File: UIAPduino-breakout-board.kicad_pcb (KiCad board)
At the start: 2 copper layers, 56.6 x 54.1 mm, 13 parts, among them J1 Conn_01x20_Pin, J2 Conn_01x20_Socket, J3 Barrel_Jack_Switch, U3 L7805

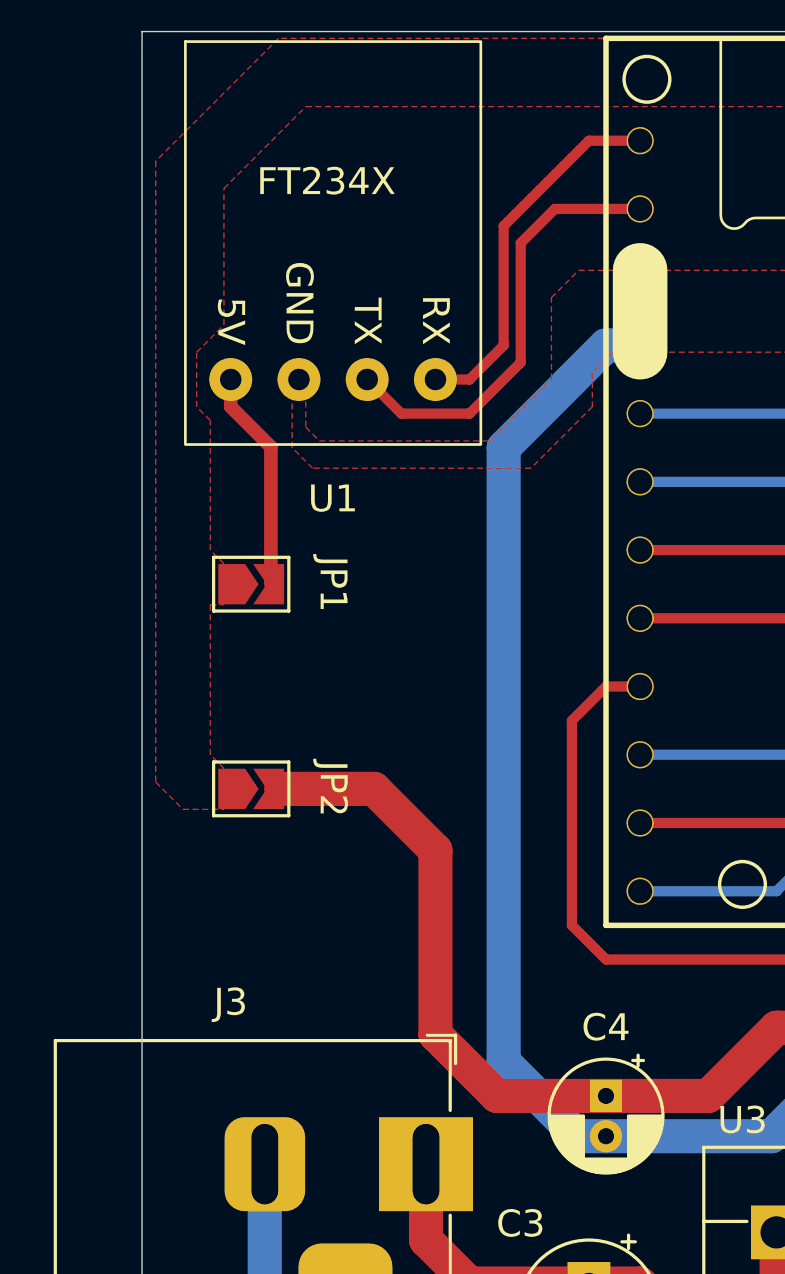
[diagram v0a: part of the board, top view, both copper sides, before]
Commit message: ジャンパをスイッチに変更
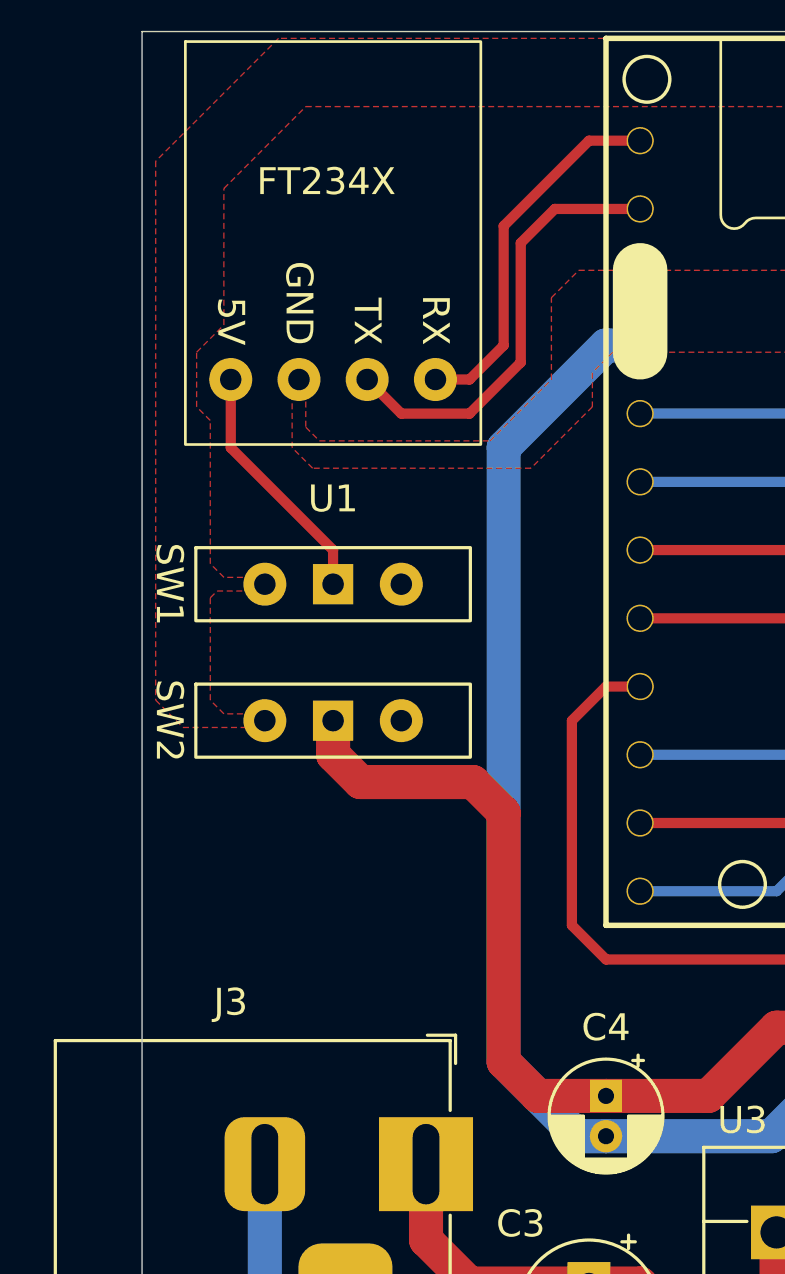
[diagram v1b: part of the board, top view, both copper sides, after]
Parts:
- removed JP1, JP2: Jumper_2_Open, Jumper:SolderJumper-2_P1.3mm_Open_TrianglePad1.0x1.5mm
- added SW1: SW_SPDT_312, Button_Switch_THT:SW_Slide-03_Wuerth-WS-SLTV_10x2.5x6.4_P2.54mm, F.Cu at (133.3, 83.8)
- added SW2: SW_SPDT_312, Button_Switch_THT:SW_Slide-03_Wuerth-WS-SLTV_10x2.5x6.4_P2.54mm, F.Cu at (133.3, 88.9)
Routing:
- net Net-(D1-A): track 45.1 -> 46.3 mm
- net Net-(SW1-B): track 8.24 -> 9.20 mm

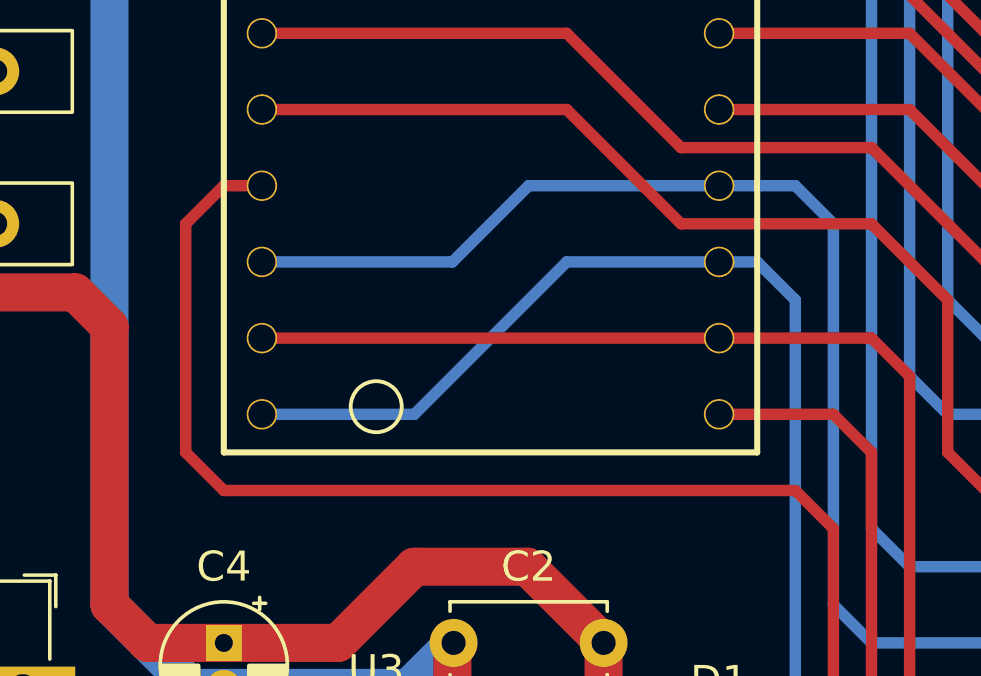
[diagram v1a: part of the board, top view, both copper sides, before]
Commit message: なくていい配線を削除
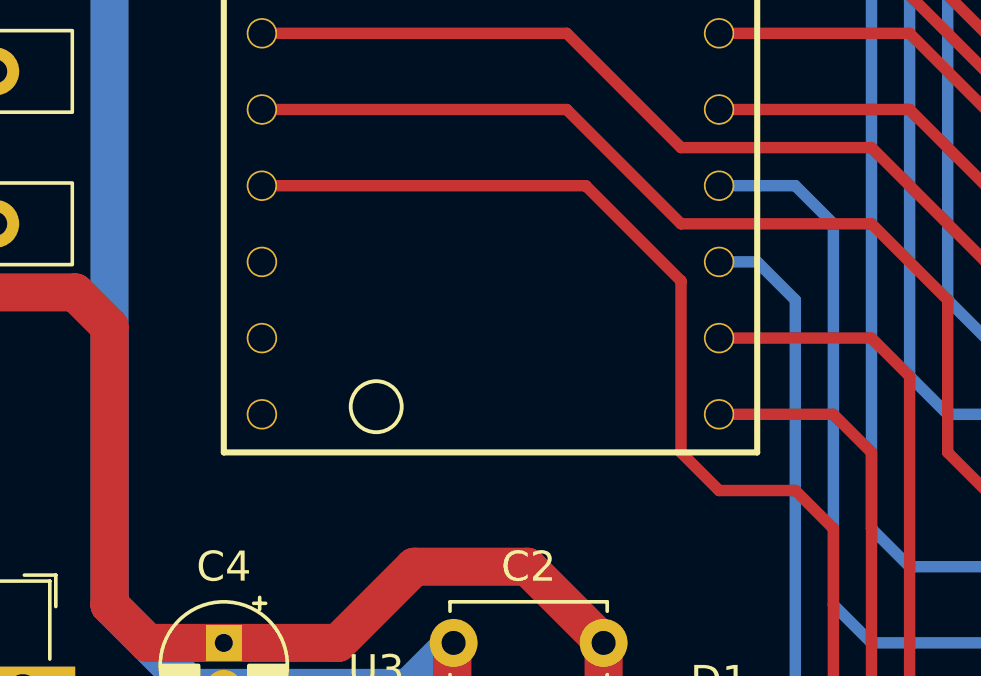
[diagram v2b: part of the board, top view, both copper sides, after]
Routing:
- net Net-(J1-Pin_17): track 55.2 -> 37.9 mm
- net Net-(J1-Pin_15): track 51.6 -> 35.3 mm
- net Net-(J1-Pin_16): track 48.0 -> 32.8 mm
- net Net-(J1-Pin_19): track 64.3 -> 58.1 mm
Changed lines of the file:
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@@
-	)
-	(segment
-		(start 144.78 90.17)
-		(end 151.13 90.17)
-		(width 0.381)
-		(layer "B.Cu")
-		(net 4)
 	)
 	(segment
@@
 	)
 	(segment
-		(start 153.67 87.63)
-		(end 160.02 87.63)
-		(width 0.381)
-		(layer "B.Cu")
-		(net 4)
-	)
-	(segment
-		(start 151.13 90.17)
-		(end 153.67 87.63)
-		(width 0.381)
-		(layer "B.Cu")
-		(net 4)
-	)
-	(segment
 		(start 171.45 102.87)
 		(end 165.1 102.87)
@@
 	)
 	(segment
+		(start 144.78 87.63)
+		(end 155.575 87.63)
+		(width 0.381)
+		(layer "F.Cu")
+		(net 6)
+	)
+	(segment
+		(start 160.02 97.79)
+		(end 162.56 97.79)
+		(width 0.381)
+		(layer "F.Cu")
+		(net 6)
+	)
+	(segment
+		(start 155.575 87.63)
+		(end 158.75 90.805)
+		(width 0.381)
+		(layer "F.Cu")
+		(net 6)
+	)
+	(segment
+		(start 163.83 99.06)
+		(end 163.83 111.76)
+		(width 0.381)
+		(layer "F.Cu")
+		(net 6)
+	)
+	(segment
 		(start 163.83 111.76)
 		(end 165.1 113.03)
@@
 	)
 	(segment
-		(start 144.78 87.63)
-		(end 143.51 87.63)
-		(width 0.381)
-		(layer "F.Cu")
-		(net 6)
-	)
-	(segment
-		(start 142.24 88.9)
-		(end 142.24 96.520168)
-		(width 0.381)
-		(layer "F.Cu")
-		(net 6)
-	)
-	(segment
-		(start 143.51 87.63)
-		(end 142.24 88.9)
-		(width 0.381)
-		(layer "F.Cu")
-		(net 6)
-	)
-	(segment
-		(start 142.24 96.520168)
-		(end 143.509832 97.79)
+		(start 158.75 90.805)
+		(end 158.75 96.52)
+		(width 0.381)
+		(layer "F.Cu")
+		(net 6)
+	)
+	(segment
+		(start 165.1 113.03)
+		(end 171.45 113.03)
 		(width 0.381)
 		(layer "F.Cu")
@@
 	)
 	(segment
-		(start 162.56 97.79)
-		(end 143.509832 97.79)
-		(width 0.381)
-		(layer "F.Cu")
-		(net 6)
-	)
-	(segment
-		(start 165.1 113.03)
-		(end 171.45 113.03)
-		(width 0.381)
-		(layer "F.Cu")
-		(net 6)
-	)
-	(segment
-		(start 163.83 99.06)
-		(end 163.83 111.76)
+		(start 158.75 96.52)
+		(end 160.02 97.79)
 		(width 0.381)
 		(layer "F.Cu")
@@
 	)
 	(segment
-		(start 154.94 90.17)
-		(end 149.86 95.25)
-		(width 0.381)
-		(layer "B.Cu")
-		(net 12)
-	)
-	(segment
 		(start 160.02 90.17)
 		(end 161.29 90.17)
@@
 	)
 	(segment
-		(start 160.02 90.17)
-		(end 154.94 90.17)
-		(width 0.381)
-		(layer "B.Cu")
-		(net 12)
-	)
-	(segment
 		(start 162.56 106.68)
 		(end 162.56 91.44)
@@
 	)
 	(segment
-		(start 149.86 95.25)
-		(end 144.78 95.25)
-		(width 0.381)
-		(layer "B.Cu")
-		(net 12)
-	)
-	(segment
 		(start 171.45 110.49)
 		(end 166.37 110.49)
@@
 		(width 0.381)
 		(layer "F.Cu")
-		(net 14)
-	)
-	(segment
-		(start 160.02 92.71)
-		(end 144.78 92.71)
-		(width 0.381)
-		(layer "F.Cu")

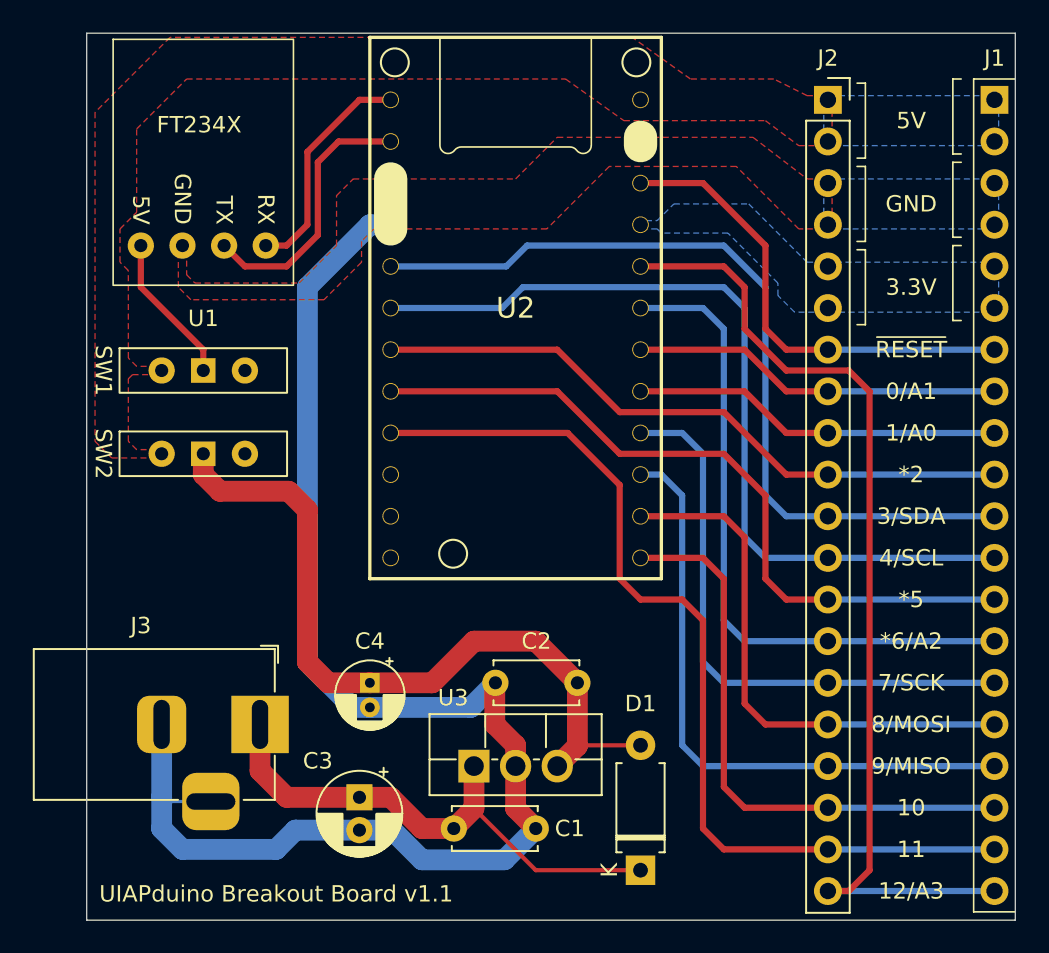
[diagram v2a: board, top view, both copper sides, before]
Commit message: UART 接続先切り替え用スイッチを追加
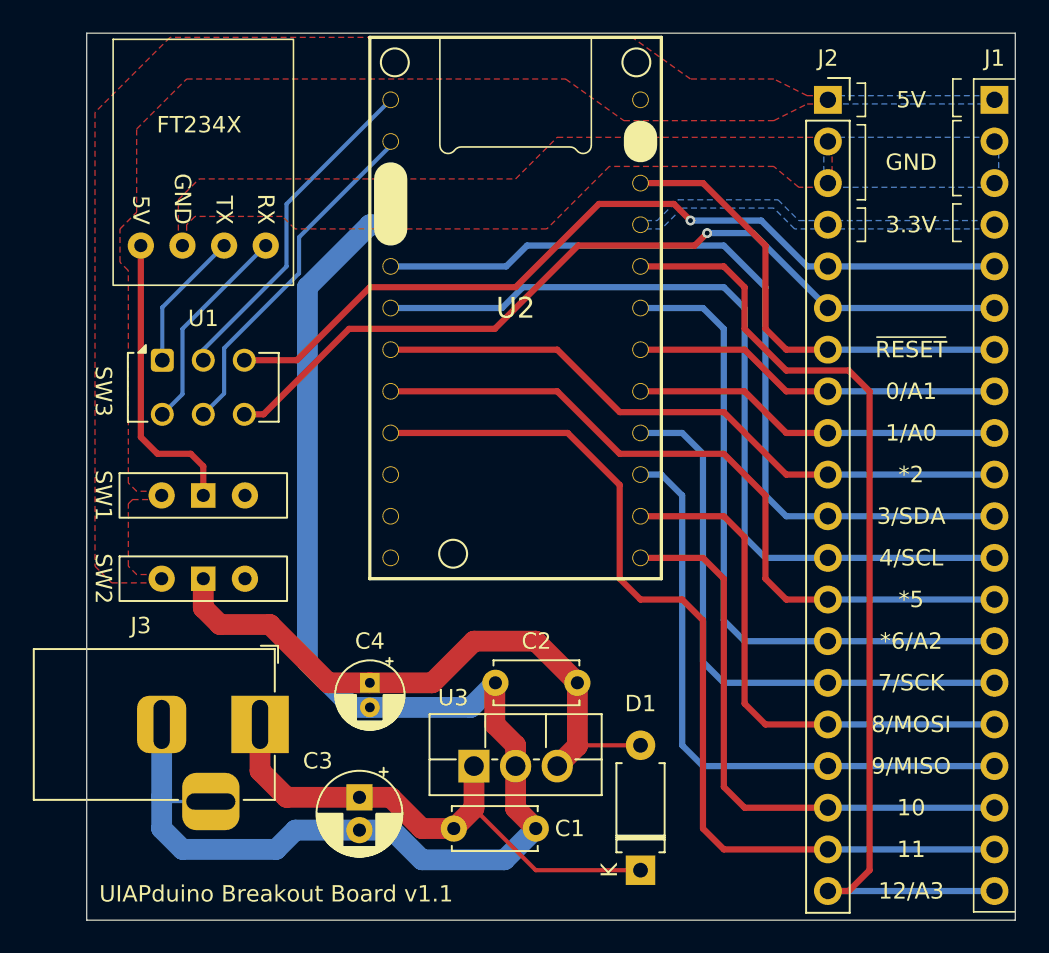
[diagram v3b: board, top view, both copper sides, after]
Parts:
- added SW3: SW_Slide_DPDT, Button_Switch_THT:SW_CK_JS202011CQN_DPDT_Straight, F.Cu at (130.8, 83.2)
- moved SW1 7.62 mm to (133.3, 91.4)
- moved SW2 7.62 mm to (133.3, 96.5)
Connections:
- J1 pad 2: +5V -> GND
- J1 pad 4: GND -> +3.3V
- J1 pad 5: +3.3V -> /EXT_TX
- J1 pad 6: +3.3V -> /EXT_RX
- J2 pad 2: +5V -> GND
- J2 pad 4: GND -> +3.3V
- J2 pad 5: +3.3V -> /EXT_TX
- J2 pad 6: +3.3V -> /EXT_RX
- U1 pad 3: Net-(U1-TX) -> /USB_TX
- U1 pad 4: Net-(U1-RX) -> /USB_RX
- U2 pad 1: Net-(U1-RX) -> /UIAP_TX
- U2 pad 2: Net-(U1-TX) -> /UIAP_RX
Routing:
- net /EXT_RX: track 0.00 -> 52.2 mm, vias 0 -> 1
- net /EXT_TX: track 0.00 -> 51.4 mm, vias 0 -> 1
- net /UIAP_RX: track 0.00 -> 21.4 mm
- net /UIAP_TX: track 0.00 -> 20.6 mm
- net Net-(U1-TX): track 16.4 -> 0.00 mm
- net Net-(U1-RX): track 13.9 -> 0.00 mm
- net /USB_RX: track 0.00 -> 12.9 mm
- net Net-(SW1-B): track 9.20 -> 18.0 mm
- net /USB_TX: track 0.00 -> 8.56 mm
- net Net-(D1-A): track 46.3 -> 38.1 mm

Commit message: 電源配線ちょい弄り
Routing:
- net GND: track 87.5 -> 80.5 mm
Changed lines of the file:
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@@
 	)
 	(segment
-		(start 131.065 110.11)
-		(end 130.81 109.855)
-		(width 0.2)
-		(layer "B.Cu")
-		(net 3)
-	)
-	(segment
-		(start 137.795 113.03)
-		(end 138.97 111.855)
-		(width 1.27)
-		(layer "B.Cu")
-		(net 3)
-	)
-	(segment
-		(start 130.81 109.855)
-		(end 130.81 111.76)
-		(width 1.27)
-		(layer "B.Cu")
-		(net 3)
-	)
-	(segment
-		(start 138.97 111.855)
+		(start 143.51 74.93)
+		(end 144.78 74.93)
+		(width 1.27)
+		(layer "B.Cu")
+		(net 3)
+	)
+	(segment
+		(start 139.541 111.855)
 		(end 142.875 111.855)
 		(width 1.27)
@@
 	)
 	(segment
-		(start 139.7 78.74)
-		(end 143.51 74.93)
+		(start 142.47 104.37)
+		(end 141.224 103.124)
+		(width 1.27)
+		(layer "B.Cu")
+		(net 3)
+	)
+	(segment
+		(start 130.81 105.41)
+		(end 130.81 108.966)
+		(width 1.27)
+		(layer "B.Cu")
+		(net 3)
+	)
+	(segment
+		(start 130.81 108.966)
+		(end 131.954 110.11)
 		(width 1.27)
 		(layer "B.Cu")
@@
 	)
 	(segment
-		(start 132.08 113.03)
-		(end 137.795 113.03)
-		(width 1.27)
-		(layer "B.Cu")
-		(net 3)
-	)
-	(segment
-		(start 133.81 110.11)
-		(end 131.065 110.11)
-		(width 0.2)
-		(layer "B.Cu")
-		(net 3)
-	)
-	(segment
-		(start 139.7 101.6)
-		(end 139.7 78.74)
-		(width 1.27)
-		(layer "B.Cu")
-		(net 3)
-	)
-	(segment
-		(start 130.81 105.41)
-		(end 130.81 109.855)
-		(width 1.27)
-		(layer "B.Cu")
-		(net 3)
-	)
-	(segment
-		(start 142.47 104.37)
-		(end 139.7 101.6)
+		(start 141.224 103.124)
+		(end 141.224 77.216)
+		(width 1.27)
+		(layer "B.Cu")
+		(net 3)
+	)
+	(segment
+		(start 141.224 77.216)
+		(end 143.51 74.93)
 		(width 1.27)
 		(layer "B.Cu")
@@
 	)
 	(segment
+		(start 131.954 110.11)
+		(end 137.796 110.11)
+		(width 1.27)
+		(layer "B.Cu")
+		(net 3)
+	)
+	(segment
+		(start 146.685 113.665)
+		(end 151.725 113.665)
+		(width 1.27)
+		(layer "B.Cu")
+		(net 3)
+	)
+	(segment
+		(start 137.796 110.11)
+		(end 139.541 111.855)
+		(width 1.27)
+		(layer "B.Cu")
+		(net 3)
+	)
+	(segment
 		(start 143.51 104.37)
 		(end 142.47 104.37)
@@
 	)
 	(segment
-		(start 146.685 113.665)
-		(end 151.725 113.665)
-		(width 1.27)
-		(layer "B.Cu")
-		(net 3)
-	)
-	(segment
-		(start 143.51 74.93)
-		(end 144.78 74.93)
-		(width 1.27)
-		(layer "B.Cu")
-		(net 3)
-	)
-	(segment
 		(start 151.17 102.87)
 		(end 149.67 104.37)
@@
 	)
 	(segment
-		(start 130.81 111.76)
-		(end 132.08 113.03)
-		(width 1.27)
-		(layer "B.Cu")
-		(net 3)
-	)
-	(segment
 		(start 160.02 87.63)
 		(end 162.56 87.63)
@@
 	)
 	(segment
+		(start 138.938 73.152)
+		(end 138.938 76.962)
+		(width 0.254)
+		(layer "B.Cu")
+		(net 23)
+	)
+	(segment
+		(start 138.938 76.962)
+		(end 133.35 82.55)
+		(width 0.254)
+		(layer "B.Cu")
+		(net 23)
+	)
+	(segment
+		(start 144.78 67.31)
+		(end 138.938 73.152)
+		(width 0.254)
+		(layer "B.Cu")
+		(net 23)
+	)
+	(segment
 		(start 133.35 82.55)
 		(end 133.35 83.1935)
@@
 	)
 	(segment
-		(start 144.78 67.31)
-		(end 138.43 73.66)
-		(width 0.254)
-		(layer "B.Cu")
-		(net 23)
-	)
-	(segment
-		(start 138.43 73.66)
-		(end 138.43 77.47)
-		(width 0.254)
-		(layer "B.Cu")
-		(net 23)
-	)
-	(segment
-		(start 138.43 77.47)
-		(end 133.35 82.55)
-		(width 0.254)
-		(layer "B.Cu")
-		(net 23)
-	)
-	(segment
-		(start 139.192 77.887527)
-		(end 134.62 82.459527)
+		(start 139.7 75.184)
+		(end 139.7 77.379527)
 		(width 0.254)
 		(layer "B.Cu")
@@
 	)
 	(segment
-		(start 139.192 75.692)
-		(end 139.192 77.887527)
+		(start 144.78 69.85)
+		(end 144.78 70.104)
 		(width 0.254)
 		(layer "B.Cu")
@@
 	(segment
 		(start 144.78 70.104)
-		(end 139.192 75.692)
+		(end 139.7 75.184)
+		(width 0.254)
+		(layer "B.Cu")
+		(net 24)
+	)
+	(segment
+		(start 139.7 77.379527)
+		(end 134.62 82.459527)
 		(width 0.254)
 		(layer "B.Cu")
@@
 		(width 0.254)
 		(layer "B.Cu")
-		(net 24)
-	)
-	(segment
-		(start 144.78 69.85)
-		(end 144.78 70.104)
-		(width 0.254)
-		(layer "B.Cu")
